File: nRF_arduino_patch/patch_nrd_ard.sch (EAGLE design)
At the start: 16 parts, among them IC1 3.3V

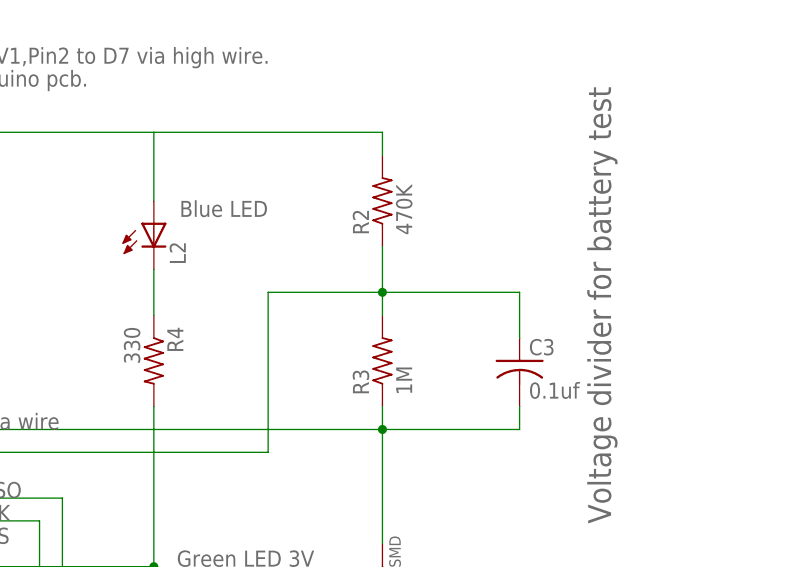
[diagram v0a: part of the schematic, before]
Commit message: nRF_arduino_patch: Fixed swapped values on R2/R3
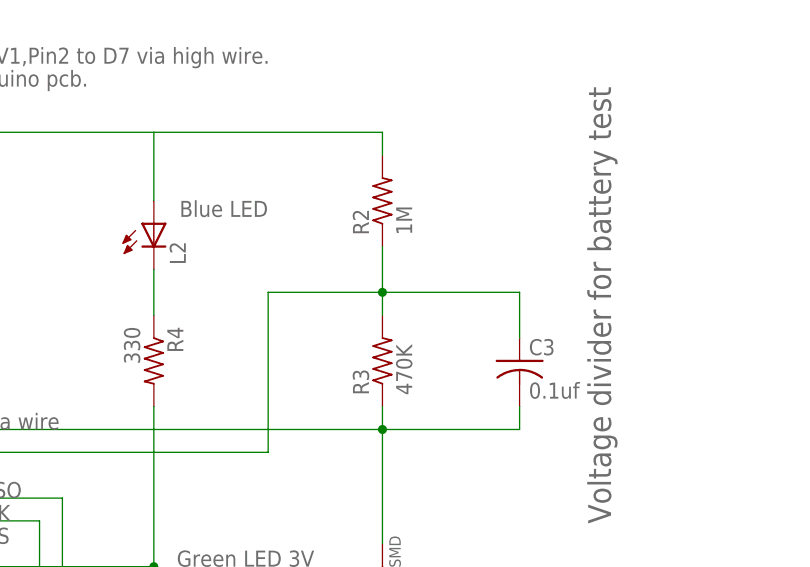
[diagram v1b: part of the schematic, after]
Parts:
- R2: value 470K -> 1M
- R3: value 1M -> 470K
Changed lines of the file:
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@@
 <part name="BAT+" library="1AA_Stofer" deviceset="SOLDER_POINT" device="A"/>
 <part name="BAT-" library="1AA_Stofer" deviceset="SOLDER_POINT" device="A"/>
-<part name="R2" library="rcl" deviceset="R-US_" device="R0603" value="470K"/>
-<part name="R3" library="rcl" deviceset="R-US_" device="R0603" value="1M"/>
+<part name="R2" library="rcl" deviceset="R-US_" device="R0603" value="1M"/>
+<part name="R3" library="rcl" deviceset="R-US_" device="R0603" value="470K"/>
 <part name="L2" library="led" deviceset="LED" device="SML0603"/>
 <part name="R4" library="rcl" deviceset="R-US_" device="R0603" value="330"/>
